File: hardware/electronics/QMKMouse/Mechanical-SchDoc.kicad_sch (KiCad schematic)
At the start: 33 parts

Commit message: update schematic from PCB; sync netlist and fix some symbol orientations; also fix LED symbol
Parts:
- MCH.FID.1, MCH.FID.2: footprint Fiducial:Fiducial_1mm_Mask2mm -> Mechanical.PcbLib:FIDUCIAL_1.5
- MCH.LOGO.2: footprint Mouse_Parts:XY - Coordinate System Marker -> Graphics.PcbLib:Coordinate System
- MCH.SP.1, MCH.SP.10, MCH.SP.11, MCH.SP.12, MCH.SP.13, MCH.SP.14, MCH.SP.15, MCH.SP.16, MCH.SP.17, MCH.SP.18, MCH.SP.19, MCH.SP.2, MCH.SP.20, MCH.SP.21, MCH.SP.22, MCH.SP.23, MCH.SP.24, MCH.SP.25, MCH.SP.26, MCH.SP.27, MCH.SP.28, MCH.SP.3, MCH.SP.4, MCH.SP.5, MCH.SP.6, MCH.SP.7, MCH.SP.8, MCH.SP.9: footprint Mouse_Parts:Spark gap -> PCBFeatures.PcbLib:SparkGap
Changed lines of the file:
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@@
       (effects (font (size 1.27 1.27)) hide)
     )
-    (property "Footprint" "Mouse_Parts:Spark gap" (id 2) (at 180.34 109.22 0)
+    (property "Footprint" "PCBFeatures.PcbLib:SparkGap" (id 2) (at 180.34 109.22 0)
       (effects (font (size 1.27 1.27)) hide)
     )
@@
       (effects (font (size 1.27 1.27)) hide)
     )
-    (property "Footprint" "Mouse_Parts:Spark gap" (id 2) (at 187.96 109.22 0)
+    (property "Footprint" "PCBFeatures.PcbLib:SparkGap" (id 2) (at 187.96 109.22 0)
       (effects (font (size 1.27 1.27)) hide)
     )
@@
       (effects (font (size 1.27 1.27)) hide)
     )
-    (property "Footprint" "Mouse_Parts:Spark gap" (id 2) (at 170.18 83.82 0)
+    (property "Footprint" "PCBFeatures.PcbLib:SparkGap" (id 2) (at 170.18 83.82 0)
       (effects (font (size 1.27 1.27)) hide)
     )
@@
       (effects (font (size 1.27 1.27)) hide)
     )
-    (property "Footprint" "Mouse_Parts:Spark gap" (id 2) (at 187.96 134.62 0)
+    (property "Footprint" "PCBFeatures.PcbLib:SparkGap" (id 2) (at 187.96 134.62 0)
       (effects (font (size 1.27 1.27)) hide)
     )
@@
       (effects (font (size 1.27 1.27)) (justify left))
     )
-    (property "Footprint" "Fiducial:Fiducial_1mm_Mask2mm" (id 2) (at 73.66 53.34 0)
+    (property "Footprint" "Mechanical.PcbLib:FIDUCIAL_1.5" (id 2) (at 73.66 53.34 0)
       (effects (font (size 1.27 1.27)) hide)
     )
@@
       (effects (font (size 1.27 1.27)) hide)
     )
-    (property "Footprint" "Mouse_Parts:Spark gap" (id 2) (at 151.13 83.82 0)
+    (property "Footprint" "PCBFeatures.PcbLib:SparkGap" (id 2) (at 151.13 83.82 0)
       (effects (font (size 1.27 1.27)) hide)
     )
@@
       (effects (font (size 1.27 1.27)) hide)
     )
-    (property "Footprint" "Mouse_Parts:Spark gap" (id 2) (at 158.75 83.82 0)
+    (property "Footprint" "PCBFeatures.PcbLib:SparkGap" (id 2) (at 158.75 83.82 0)
       (effects (font (size 1.27 1.27)) hide)
     )
@@
       (effects (font (size 1.27 1.27)) hide)
     )
-    (property "Footprint" "Mouse_Parts:Spark gap" (id 2) (at 135.89 83.82 0)
+    (property "Footprint" "PCBFeatures.PcbLib:SparkGap" (id 2) (at 135.89 83.82 0)
       (effects (font (size 1.27 1.27)) hide)
     )
@@
       (effects (font (size 1.27 1.27)) hide)
     )
-    (property "Footprint" "Mouse_Parts:Spark gap" (id 2) (at 157.48 134.62 0)
+    (property "Footprint" "PCBFeatures.PcbLib:SparkGap" (id 2) (at 157.48 134.62 0)
       (effects (font (size 1.27 1.27)) hide)
     )
@@
       (effects (font (size 1.27 1.27)) hide)
     )
-    (property "Footprint" "Mouse_Parts:Spark gap" (id 2) (at 173.99 83.82 0)
+    (property "Footprint" "PCBFeatures.PcbLib:SparkGap" (id 2) (at 173.99 83.82 0)
       (effects (font (size 1.27 1.27)) hide)
     )
@@
       (effects (font (size 1.27 1.27)) hide)
     )
-    (property "Footprint" "Mouse_Parts:Spark gap" (id 2) (at 165.1 134.62 0)
+    (property "Footprint" "PCBFeatures.PcbLib:SparkGap" (id 2) (at 165.1 134.62 0)
       (effects (font (size 1.27 1.27)) hide)
     )
@@
       (effects (font (size 1.27 1.27)) hide)
     )
-    (property "Footprint" "Mouse_Parts:Spark gap" (id 2) (at 153.67 134.62 0)
+    (property "Footprint" "PCBFeatures.PcbLib:SparkGap" (id 2) (at 153.67 134.62 0)
       (effects (font (size 1.27 1.27)) hide)
     )
@@
       (effects (font (size 1.27 1.27)) hide)
     )
-    (property "Footprint" "Mouse_Parts:Spark gap" (id 2) (at 153.67 109.22 0)
+    (property "Footprint" "PCBFeatures.PcbLib:SparkGap" (id 2) (at 153.67 109.22 0)
       (effects (font (size 1.27 1.27)) hide)
     )
@@
       (effects (font (size 1.27 1.27)) hide)
     )
-    (property "Footprint" "Mouse_Parts:Spark gap" (id 2) (at 181.61 83.82 0)
+    (property "Footprint" "PCBFeatures.PcbLib:SparkGap" (id 2) (at 181.61 83.82 0)
       (effects (font (size 1.27 1.27)) hide)
     )
@@
       (effects (font (size 1.27 1.27)) hide)
     )
-    (property "Footprint" "Mouse_Parts:Spark gap" (id 2) (at 147.32 83.82 0)
+    (property "Footprint" "PCBFeatures.PcbLib:SparkGap" (id 2) (at 147.32 83.82 0)
       (effects (font (size 1.27 1.27)) hide)
     )
@@
       (effects (font (size 1.27 1.27)) hide)
     )
-    (property "Footprint" "Mouse_Parts:Spark gap" (id 2) (at 191.77 109.22 0)
+    (property "Footprint" "PCBFeatures.PcbLib:SparkGap" (id 2) (at 191.77 109.22 0)
       (effects (font (size 1.27 1.27)) hide)
     )
@@
       (effects (font (size 1.27 1.27)) hide)
     )
-    (property "Footprint" "Mouse_Parts:Spark gap" (id 2) (at 168.91 109.22 0)
+    (property "Footprint" "PCBFeatures.PcbLib:SparkGap" (id 2) (at 168.91 109.22 0)
       (effects (font (size 1.27 1.27)) hide)
     )
@@
       (effects (font (size 1.27 1.27)) hide)
     )
-    (property "Footprint" "Mouse_Parts:Spark gap" (id 2) (at 196.85 83.82 0)
+    (property "Footprint" "PCBFeatures.PcbLib:SparkGap" (id 2) (at 196.85 83.82 0)
       (effects (font (size 1.27 1.27)) hide)
     )
@@
       (effects (font (size 1.27 1.27)) hide)
     )
-    (property "Footprint" "Mouse_Parts:Spark gap" (id 2) (at 176.53 109.22 0)
+    (property "Footprint" "PCBFeatures.PcbLib:SparkGap" (id 2) (at 176.53 109.22 0)
       (effects (font (size 1.27 1.27)) hide)
     )
@@
       (effects (font (size 1.27 1.27)) (justify left))
     )
-    (property "Footprint" "Fiducial:Fiducial_1mm_Mask2mm" (id 2) (at 54.61 53.34 0)
+    (property "Footprint" "Mechanical.PcbLib:FIDUCIAL_1.5" (id 2) (at 54.61 53.34 0)
       (effects (font (size 1.27 1.27)) hide)
     )
@@
       (effects (font (size 1.27 1.27)) hide)
     )
-    (property "Footprint" "Mouse_Parts:Spark gap" (id 2) (at 193.04 83.82 0)
+    (property "Footprint" "PCBFeatures.PcbLib:SparkGap" (id 2) (at 193.04 83.82 0)
       (effects (font (size 1.27 1.27)) hide)
     )
@@
       (effects (font (size 1.27 1.27)) hide)
     )
-    (property "Footprint" "Mouse_Parts:Spark gap" (id 2) (at 157.48 109.22 0)
+    (property "Footprint" "PCBFeatures.PcbLib:SparkGap" (id 2) (at 157.48 109.22 0)
       (effects (font (size 1.27 1.27)) hide)
     )
@@
       (effects (font (size 1.27 1.27)) hide)
     )
-    (property "Footprint" "Mouse_Parts:Spark gap" (id 2) (at 168.91 134.62 0)
+    (property "Footprint" "PCBFeatures.PcbLib:SparkGap" (id 2) (at 168.91 134.62 0)
       (effects (font (size 1.27 1.27)) hide)
     )
@@
       (effects (font (size 1.27 1.27)) (justify left))
     )
-    (property "Footprint" "Mouse_Parts:XY - Coordinate System Marker" (id 2) (at 73.66 90.17 0)
+    (property "Footprint" "Graphics.PcbLib:Coordinate System" (id 2) (at 73.66 90.17 0)
       (effects (font (size 1.27 1.27)) hide)
     )
@@
       (effects (font (size 1.27 1.27)) hide)
     )
-    (property "Footprint" "Mouse_Parts:Spark gap" (id 2) (at 191.77 134.62 0)
+    (property "Footprint" "PCBFeatures.PcbLib:SparkGap" (id 2) (at 191.77 134.62 0)
       (effects (font (size 1.27 1.27)) hide)
     )
@@
       (effects (font (size 1.27 1.27)) hide)
     )
-    (property "Footprint" "Mouse_Parts:Spark gap" (id 2) (at 185.42 83.82 0)
+    (property "Footprint" "PCBFeatures.PcbLib:SparkGap" (id 2) (at 185.42 83.82 0)
       (effects (font (size 1.27 1.27)) hide)
     )
@@
       (effects (font (size 1.27 1.27)) hide)
     )
-    (property "Footprint" "Mouse_Parts:Spark gap" (id 2) (at 162.56 83.82 0)
+    (property "Footprint" "PCBFeatures.PcbLib:SparkGap" (id 2) (at 162.56 83.82 0)
       (effects (font (size 1.27 1.27)) hide)
     )
@@
       (effects (font (size 1.27 1.27)) hide)
     )
-    (property "Footprint" "Mouse_Parts:Spark gap" (id 2) (at 165.1 109.22 0)
+    (property "Footprint" "PCBFeatures.PcbLib:SparkGap" (id 2) (at 165.1 109.22 0)
       (effects (font (size 1.27 1.27)) hide)
     )
@@
       (effects (font (size 1.27 1.27)) hide)
     )
-    (property "Footprint" "Mouse_Parts:Spark gap" (id 2) (at 139.7 83.82 0)
+    (property "Footprint" "PCBFeatures.PcbLib:SparkGap" (id 2) (at 139.7 83.82 0)
       (effects (font (size 1.27 1.27)) hide)
     )
@@
       (effects (font (size 1.27 1.27)) hide)
     )
-    (property "Footprint" "Mouse_Parts:Spark gap" (id 2) (at 180.34 134.62 0)
+    (property "Footprint" "PCBFeatures.PcbLib:SparkGap" (id 2) (at 180.34 134.62 0)
       (effects (font (size 1.27 1.27)) hide)
     )
@@
       (effects (font (size 1.27 1.27)) hide)
     )
-    (property "Footprint" "Mouse_Parts:Spark gap" (id 2) (at 176.53 134.62 0)
-      (effects (font (size 1.27 1.27)) hide)
-    )
+    (property "Footprint" "PCBFeatures.PcbLib:SparkGap" (id 2) (at 176.53 134.62 0)
+      (effects (font (size 1.27 1.27)) hide)
+    )

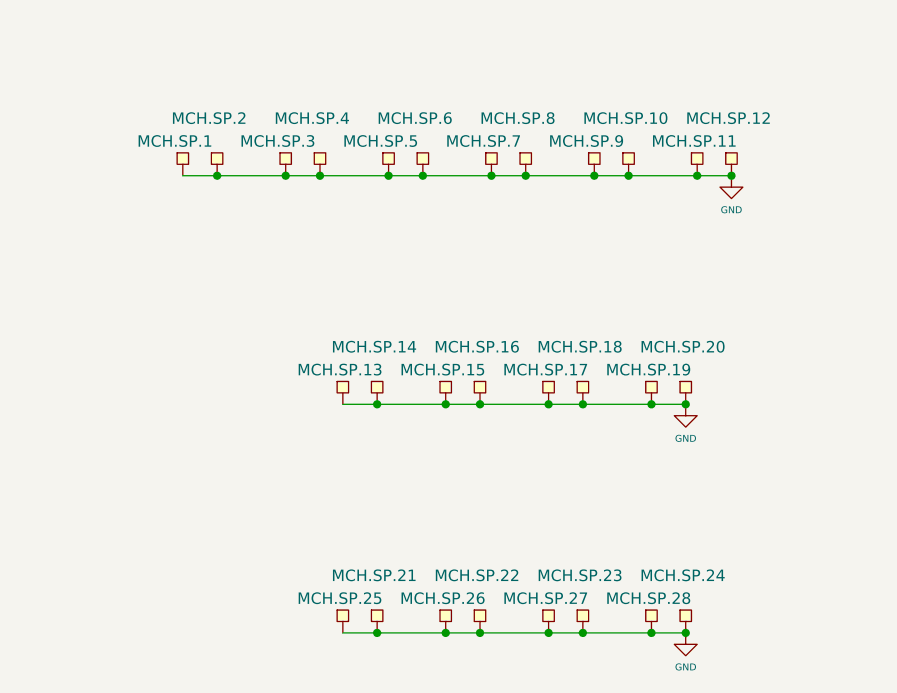
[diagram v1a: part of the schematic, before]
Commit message: Fix some schematic PCB mismatch
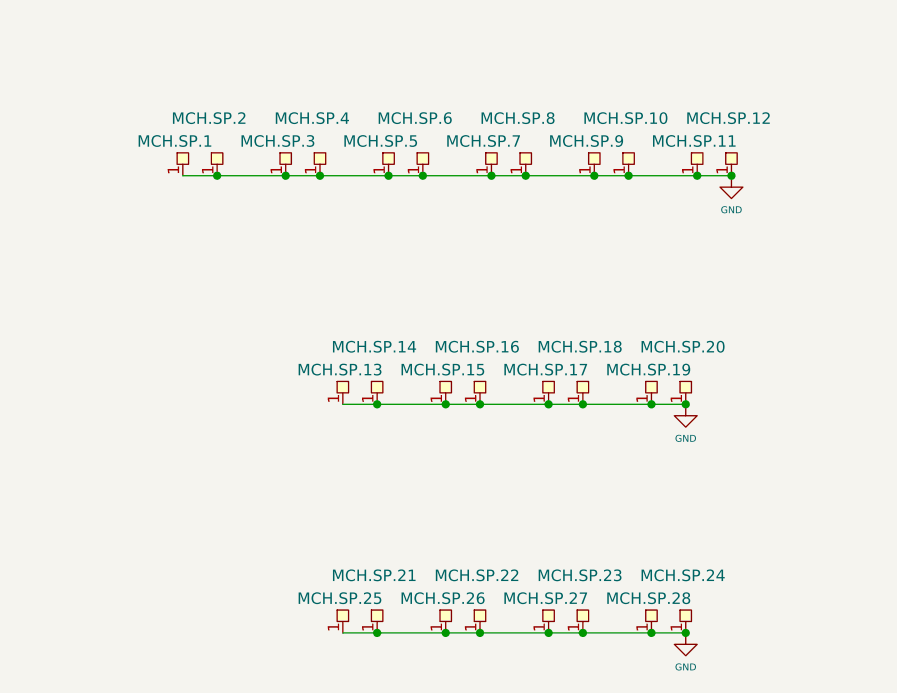
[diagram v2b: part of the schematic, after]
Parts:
- MCH.SP.1, MCH.SP.10, MCH.SP.11, MCH.SP.12, MCH.SP.13, MCH.SP.14, MCH.SP.15, MCH.SP.16, MCH.SP.17, MCH.SP.18, MCH.SP.19, MCH.SP.2, MCH.SP.20, MCH.SP.21, MCH.SP.22, MCH.SP.23, MCH.SP.24, MCH.SP.25, MCH.SP.26, MCH.SP.27, MCH.SP.28, MCH.SP.3, MCH.SP.4, MCH.SP.5, MCH.SP.6, MCH.SP.7, MCH.SP.8, MCH.SP.9: footprint PCBFeatures.PcbLib:SparkGap -> Mouse_Parts:Spark gap
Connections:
- net GND: now also MCH.SP.1.1, MCH.SP.10.1, MCH.SP.11.1, MCH.SP.12.1, MCH.SP.13.1, MCH.SP.14.1, MCH.SP.15.1, MCH.SP.16.1, MCH.SP.17.1, MCH.SP.18.1, MCH.SP.19.1, MCH.SP.2.1, MCH.SP.20.1, MCH.SP.21.1, MCH.SP.22.1, MCH.SP.23.1, MCH.SP.24.1, MCH.SP.25.1, MCH.SP.26.1, MCH.SP.27.1, MCH.SP.28.1, MCH.SP.3.1, MCH.SP.4.1, MCH.SP.5.1, MCH.SP.6.1, MCH.SP.7.1, MCH.SP.8.1, MCH.SP.9.1; no longer MCH.SP.1., MCH.SP.10., MCH.SP.11., MCH.SP.12., MCH.SP.13., MCH.SP.14., MCH.SP.15., MCH.SP.16., MCH.SP.17., MCH.SP.18., MCH.SP.19., MCH.SP.2., MCH.SP.20., MCH.SP.21., MCH.SP.22., MCH.SP.23., MCH.SP.24., MCH.SP.25., MCH.SP.26., MCH.SP.27., MCH.SP.28., MCH.SP.3., MCH.SP.4., MCH.SP.5., MCH.SP.6., MCH.SP.7., MCH.SP.8., MCH.SP.9.

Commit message: Fix all remaining DRC errors and schematic mismatches
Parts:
- MCH.FID.1, MCH.FID.2: symbol Mechanical:Fiducial -> Mouse_Parts:Fiducial
- MCH.SP.1, MCH.SP.10, MCH.SP.11, MCH.SP.12, MCH.SP.13, MCH.SP.14, MCH.SP.15, MCH.SP.16, MCH.SP.17, MCH.SP.18, MCH.SP.19, MCH.SP.2, MCH.SP.20, MCH.SP.21, MCH.SP.22, MCH.SP.23, MCH.SP.24, MCH.SP.25, MCH.SP.26, MCH.SP.27, MCH.SP.28, MCH.SP.3, MCH.SP.4, MCH.SP.5, MCH.SP.6, MCH.SP.7, MCH.SP.8, MCH.SP.9: footprint Mouse_Parts:Spark gap -> PCBFeatures.PcbLib:SparkGap
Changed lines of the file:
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@@
       (effects (font (size 1.27 1.27)) hide)
     )
-    (property "Footprint" "Mouse_Parts:Spark gap" (id 2) (at 180.34 109.22 0)
+    (property "Footprint" "PCBFeatures.PcbLib:SparkGap" (id 2) (at 180.34 109.22 0)
       (effects (font (size 1.27 1.27)) hide)
     )
@@
       (effects (font (size 1.27 1.27)) hide)
     )
-    (property "Footprint" "Mouse_Parts:Spark gap" (id 2) (at 187.96 109.22 0)
+    (property "Footprint" "PCBFeatures.PcbLib:SparkGap" (id 2) (at 187.96 109.22 0)
       (effects (font (size 1.27 1.27)) hide)
     )
@@
       (effects (font (size 1.27 1.27)) hide)
     )
-    (property "Footprint" "Mouse_Parts:Spark gap" (id 2) (at 170.18 83.82 0)
+    (property "Footprint" "PCBFeatures.PcbLib:SparkGap" (id 2) (at 170.18 83.82 0)
       (effects (font (size 1.27 1.27)) hide)
     )
@@
       (effects (font (size 1.27 1.27)) hide)
     )
-    (property "Footprint" "Mouse_Parts:Spark gap" (id 2) (at 187.96 134.62 0)
+    (property "Footprint" "PCBFeatures.PcbLib:SparkGap" (id 2) (at 187.96 134.62 0)
       (effects (font (size 1.27 1.27)) hide)
     )
@@
     (pin "1")
   )
-  (symbol (lib_id "Mechanical:Fiducial") (at 73.66 53.34 0) (unit 1)
+  (symbol (lib_id "Mouse_Parts:Fiducial") (at 73.66 53.34 0) (unit 1)
     (in_bom yes) (on_board yes) (fields_autoplaced)
     (property "Reference" "MCH.FID.2" (id 0) (at 76.2 52.0699 0)
@@
       (effects (font (size 1.27 1.27)) hide)
     )
+    (pin "1")
   )
   (symbol (lib_id "Mechanical:MountingHole") (at 74.93 69.85 0) (unit 1)
@@
       (effects (font (size 1.27 1.27)) hide)
     )
-    (property "Footprint" "Mouse_Parts:Spark gap" (id 2) (at 151.13 83.82 0)
+    (property "Footprint" "PCBFeatures.PcbLib:SparkGap" (id 2) (at 151.13 83.82 0)
       (effects (font (size 1.27 1.27)) hide)
     )
@@
       (effects (font (size 1.27 1.27)) hide)
     )
-    (property "Footprint" "Mouse_Parts:Spark gap" (id 2) (at 158.75 83.82 0)
+    (property "Footprint" "PCBFeatures.PcbLib:SparkGap" (id 2) (at 158.75 83.82 0)
       (effects (font (size 1.27 1.27)) hide)
     )
@@
       (effects (font (size 1.27 1.27)) hide)
     )
-    (property "Footprint" "Mouse_Parts:Spark gap" (id 2) (at 135.89 83.82 0)
+    (property "Footprint" "PCBFeatures.PcbLib:SparkGap" (id 2) (at 135.89 83.82 0)
       (effects (font (size 1.27 1.27)) hide)
     )
@@
       (effects (font (size 1.27 1.27)) hide)
     )
-    (property "Footprint" "Mouse_Parts:Spark gap" (id 2) (at 157.48 134.62 0)
+    (property "Footprint" "PCBFeatures.PcbLib:SparkGap" (id 2) (at 157.48 134.62 0)
       (effects (font (size 1.27 1.27)) hide)
     )
@@
       (effects (font (size 1.27 1.27)) hide)
     )
-    (property "Footprint" "Mouse_Parts:Spark gap" (id 2) (at 173.99 83.82 0)
+    (property "Footprint" "PCBFeatures.PcbLib:SparkGap" (id 2) (at 173.99 83.82 0)
       (effects (font (size 1.27 1.27)) hide)
     )
@@
       (effects (font (size 1.27 1.27)) hide)
     )
-    (property "Footprint" "Mouse_Parts:Spark gap" (id 2) (at 165.1 134.62 0)
+    (property "Footprint" "PCBFeatures.PcbLib:SparkGap" (id 2) (at 165.1 134.62 0)
       (effects (font (size 1.27 1.27)) hide)
     )
@@
       (effects (font (size 1.27 1.27)) hide)
     )
-    (property "Footprint" "Mouse_Parts:Spark gap" (id 2) (at 153.67 134.62 0)
+    (property "Footprint" "PCBFeatures.PcbLib:SparkGap" (id 2) (at 153.67 134.62 0)
       (effects (font (size 1.27 1.27)) hide)
     )
@@
       (effects (font (size 1.27 1.27)) hide)
     )
-    (property "Footprint" "Mouse_Parts:Spark gap" (id 2) (at 153.67 109.22 0)
+    (property "Footprint" "PCBFeatures.PcbLib:SparkGap" (id 2) (at 153.67 109.22 0)
       (effects (font (size 1.27 1.27)) hide)
     )
@@
       (effects (font (size 1.27 1.27)) hide)
     )
-    (property "Footprint" "Mouse_Parts:Spark gap" (id 2) (at 181.61 83.82 0)
+    (property "Footprint" "PCBFeatures.PcbLib:SparkGap" (id 2) (at 181.61 83.82 0)
       (effects (font (size 1.27 1.27)) hide)
     )
@@
       (effects (font (size 1.27 1.27)) hide)
     )
-    (property "Footprint" "Mouse_Parts:Spark gap" (id 2) (at 147.32 83.82 0)
+    (property "Footprint" "PCBFeatures.PcbLib:SparkGap" (id 2) (at 147.32 83.82 0)
       (effects (font (size 1.27 1.27)) hide)
     )
@@
       (effects (font (size 1.27 1.27)) hide)
     )
-    (property "Footprint" "Mouse_Parts:Spark gap" (id 2) (at 191.77 109.22 0)
+    (property "Footprint" "PCBFeatures.PcbLib:SparkGap" (id 2) (at 191.77 109.22 0)
       (effects (font (size 1.27 1.27)) hide)
     )
@@
       (effects (font (size 1.27 1.27)) hide)
     )
-    (property "Footprint" "Mouse_Parts:Spark gap" (id 2) (at 168.91 109.22 0)
+    (property "Footprint" "PCBFeatures.PcbLib:SparkGap" (id 2) (at 168.91 109.22 0)
       (effects (font (size 1.27 1.27)) hide)
     )
@@
       (effects (font (size 1.27 1.27)) hide)
     )
-    (property "Footprint" "Mouse_Parts:Spark gap" (id 2) (at 196.85 83.82 0)
+    (property "Footprint" "PCBFeatures.PcbLib:SparkGap" (id 2) (at 196.85 83.82 0)
       (effects (font (size 1.27 1.27)) hide)
     )
@@
       (effects (font (size 1.27 1.27)) hide)
     )
-    (property "Footprint" "Mouse_Parts:Spark gap" (id 2) (at 176.53 109.22 0)
+    (property "Footprint" "PCBFeatures.PcbLib:SparkGap" (id 2) (at 176.53 109.22 0)
       (effects (font (size 1.27 1.27)) hide)
     )
@@
     (pin "1")
   )
-  (symbol (lib_id "Mechanical:Fiducial") (at 54.61 53.34 0) (unit 1)
+  (symbol (lib_id "Mouse_Parts:Fiducial") (at 54.61 53.34 0) (unit 1)
     (in_bom yes) (on_board yes) (fields_autoplaced)
     (property "Reference" "MCH.FID.1" (id 0) (at 57.15 52.0699 0)
@@
       (effects (font (size 1.27 1.27)) hide)
     )
+    (pin "1")
   )
   (symbol (lib_name "Spark_gap_14") (lib_id "Mouse_Parts:Spark_gap") (at 193.04 83.82 0) (unit 1)
@@
       (effects (font (size 1.27 1.27)) hide)
     )
-    (property "Footprint" "Mouse_Parts:Spark gap" (id 2) (at 193.04 83.82 0)
+    (property "Footprint" "PCBFeatures.PcbLib:SparkGap" (id 2) (at 193.04 83.82 0)
       (effects (font (size 1.27 1.27)) hide)
     )
@@
       (effects (font (size 1.27 1.27)) hide)
     )
-    (property "Footprint" "Mouse_Parts:Spark gap" (id 2) (at 157.48 109.22 0)
+    (property "Footprint" "PCBFeatures.PcbLib:SparkGap" (id 2) (at 157.48 109.22 0)
       (effects (font (size 1.27 1.27)) hide)
     )
@@
       (effects (font (size 1.27 1.27)) hide)
     )
-    (property "Footprint" "Mouse_Parts:Spark gap" (id 2) (at 168.91 134.62 0)
+    (property "Footprint" "PCBFeatures.PcbLib:SparkGap" (id 2) (at 168.91 134.62 0)
       (effects (font (size 1.27 1.27)) hide)
     )
@@
       (effects (font (size 1.27 1.27)) hide)
     )
-    (property "Footprint" "Mouse_Parts:Spark gap" (id 2) (at 191.77 134.62 0)
+    (property "Footprint" "PCBFeatures.PcbLib:SparkGap" (id 2) (at 191.77 134.62 0)
       (effects (font (size 1.27 1.27)) hide)
     )
@@
       (effects (font (size 1.27 1.27)) hide)
     )
-    (property "Footprint" "Mouse_Parts:Spark gap" (id 2) (at 185.42 83.82 0)
+    (property "Footprint" "PCBFeatures.PcbLib:SparkGap" (id 2) (at 185.42 83.82 0)
       (effects (font (size 1.27 1.27)) hide)
     )
@@
       (effects (font (size 1.27 1.27)) hide)
     )
-    (property "Footprint" "Mouse_Parts:Spark gap" (id 2) (at 162.56 83.82 0)
+    (property "Footprint" "PCBFeatures.PcbLib:SparkGap" (id 2) (at 162.56 83.82 0)
       (effects (font (size 1.27 1.27)) hide)
     )
@@
       (effects (font (size 1.27 1.27)) hide)
     )
-    (property "Footprint" "Mouse_Parts:Spark gap" (id 2) (at 165.1 109.22 0)
+    (property "Footprint" "PCBFeatures.PcbLib:SparkGap" (id 2) (at 165.1 109.22 0)
       (effects (font (size 1.27 1.27)) hide)
     )
@@
       (effects (font (size 1.27 1.27)) hide)
     )
-    (property "Footprint" "Mouse_Parts:Spark gap" (id 2) (at 139.7 83.82 0)
+    (property "Footprint" "PCBFeatures.PcbLib:SparkGap" (id 2) (at 139.7 83.82 0)
       (effects (font (size 1.27 1.27)) hide)
     )
@@
       (effects (font (size 1.27 1.27)) hide)
     )
-    (property "Footprint" "Mouse_Parts:Spark gap" (id 2) (at 180.34 134.62 0)
+    (property "Footprint" "PCBFeatures.PcbLib:SparkGap" (id 2) (at 180.34 134.62 0)
       (effects (font (size 1.27 1.27)) hide)
     )
@@
       (effects (font (size 1.27 1.27)) hide)
     )
-    (property "Footprint" "Mouse_Parts:Spark gap" (id 2) (at 176.53 134.62 0)
-      (effects (font (size 1.27 1.27)) hide)
-    )
+    (property "Footprint" "PCBFeatures.PcbLib:SparkGap" (id 2) (at 176.53 134.62 0)
+      (effects (font (size 1.27 1.27)) hide)
+    )
